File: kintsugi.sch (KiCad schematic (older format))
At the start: 147 parts

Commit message: Footprints added
First revision of the schematic finished and footprints added.
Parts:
- removed D? (x9): D_Small, symbol Device:D_Small
- removed MX? (x10): MX-NoLED, symbol MX_Alps_Hybrid:MX-NoLED
- added C1, C10, C11, C12, C13, C14, C15, C16, C2, C3, C4, C5, C6, C7, C8, C9: 100n, Capacitor_SMD:C_0805_2012Metric_Pad1.18x1.45mm_HandSolder, symbol Device:C_Small
- added D54: D_Small, Diode_THT:D_DO-35_SOD27_P7.62mm_Horizontal, symbol Device:D_Small
- added D66, D67, D68, D69, D70, D71, D72, D73, D74, D75, D76, D77, D78, D79, D80, D81: WS2812B, LED_SMD:LED_WS2812B_PLCC4_5.0x5.0mm_P3.2mm, symbol LED:WS2812B
- added J1: Conn_01x04, Connector_PinHeader_2.54mm:PinHeader_1x04_P2.54mm_Vertical, symbol Connector_Generic:Conn_01x04
- added MX53: MX-NoLED, MX_Only:MXOnly-1.75U-Hotswap, symbol MX_Alps_Hybrid:MX-NoLED
- added SW1: Rotary_Encoder_Switch, Rotary_Encoder:RotaryEncoder_Alps_EC11E-Switch_Vertical_H20mm, symbol Device:Rotary_Encoder_Switch
- D1, D10, D11, D12, D13, D14, D15, D16, D17, D18, D19, D2, D20, D21, D22, D23, D24, D25, D26, D27, D28, D29, D3, D30, D31, D32, D33, D34, D35, D36, D37, D38, D39, D4, D40, D41, D42, D43, D44, D45, D46, D47, D48, D49, D5, D50, D51, D52, D53, D55, D56, D57, D58, D59, D6, D60, D61, D62, D63, D64, D65, D7, D8, D9: renamed from D?; footprint (none) -> Diode_THT:D_DO-35_SOD27_P7.62mm_Horizontal
- MX1, MX10, MX11, MX12, MX13, MX16, MX17, MX18, MX19, MX2, MX20, MX21, MX22, MX23, MX24, MX25, MX26, MX27, MX3, MX30, MX31, MX32, MX33, MX34, MX35, MX36, MX37, MX38, MX39, MX4, MX40, MX43, MX44, MX45, MX46, MX47, MX48, MX49, MX5, MX50, MX51, MX52, MX54, MX55, MX6, MX62, MX63, MX64, MX7, MX8, MX9: renamed from MX?; footprint (none) -> MX_Only:MXOnly-1U-Hotswap
- MX14: renamed from MX?; footprint (none) -> MX_Only:MXOnly-2U-Hotswap
- MX15, MX28: renamed from MX?; footprint (none) -> MX_Only:MXOnly-1.5U-Hotswap
- MX29: renamed from MX?; footprint (none) -> MX_Only:MXOnly-1.75U-Hotswap
- MX41, MX42: renamed from MX?; footprint (none) -> MX_Only:MXOnly-2.25U-Hotswap
- MX56, MX57, MX58, MX60, MX61: renamed from MX?; footprint (none) -> MX_Only:MXOnly-1.25U-Hotswap
- MX59: renamed from MX?; footprint (none) -> MX_Only:MXOnly-6.25U-Hotswap-ReversedStabilizers
- U1: renamed from U?; footprint (none) -> Keebio-Parts:Elite-C
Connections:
- net COL11: now also MX53.1 (COL)
- net COL14: now also SW1.S2
- net ROW0: no longer D42.1 (K)
- net ROW2: now also D42.1 (K)
- net ROW3: now also D54.1 (K)
- net ENCB: now reaches U1.19 (A2/PF5)
- net ENCB: now also SW1.B
- net ENCA: now reaches U1.20 (A3/PF4)
- net ENCA: now also SW1.A
- net VCC: now reaches U1.21 (VCC)
- net VCC: now also C1.2, C10.2, C11.2, C12.2, C13.2, C14.2, C15.2, C16.2, C2.2, C3.2, C4.2, C5.2, C6.2, C7.2, C8.2, C9.2, D66.1 (VDD), D67.1 (VDD), D68.1 (VDD), D69.1 (VDD), D70.1 (VDD), D71.1 (VDD), D72.1 (VDD), D73.1 (VDD), D74.1 (VDD), D75.1 (VDD), D76.1 (VDD), D77.1 (VDD), D78.1 (VDD), D79.1 (VDD), D80.1 (VDD), D81.1 (VDD), J1.3 (Pin_3)
- net GND: now reaches U1.23 (GND)
- net GND: now also U1.3 (GND), U1.4 (GND), C1.1, C10.1, C11.1, C12.1, C13.1, C14.1, C15.1, C16.1, C2.1, C3.1, C4.1, C5.1, C6.1, C7.1, C8.1, C9.1, D66.3 (VSS), D67.3 (VSS), D68.3 (VSS), D69.3 (VSS), D70.3 (VSS), D71.3 (VSS), D72.3 (VSS), D73.3 (VSS), D74.3 (VSS), D75.3 (VSS), D76.3 (VSS), D77.3 (VSS), D78.3 (VSS), D79.3 (VSS), D80.3 (VSS), D81.3 (VSS), J1.4 (Pin_4), SW1.C
- net ULED: now reaches U1.24 (B0)
- net ULED: now also D66.4 (DIN)
- net SDA: now reaches U1.5 (2/PD1)
- net SDA: now also J1.1 (Pin_1)
- net SCL: now reaches U1.6 (3/PD0)
- net SCL: now also J1.2 (Pin_2)
- net RE: now reaches D42.2 (A)
- net RE: now also SW1.S1
- new net: D66.2 (DOUT), D67.4 (DIN)
- new net: D67.2 (DOUT), D68.4 (DIN)
- new net: D68.2 (DOUT), D69.4 (DIN)
- new net: D69.2 (DOUT), D70.4 (DIN)
- new net: D70.2 (DOUT), D71.4 (DIN)
- new net: D71.2 (DOUT), D72.4 (DIN)
- new net: D72.2 (DOUT), D73.4 (DIN)
- new net: D73.2 (DOUT), D74.4 (DIN)
- new net: D74.2 (DOUT), D75.4 (DIN)
- new net: D75.2 (DOUT), D76.4 (DIN)
- new net: D76.2 (DOUT), D77.4 (DIN)
- new net: D77.2 (DOUT), D78.4 (DIN)
- new net: D78.2 (DOUT), D79.4 (DIN)
- new net: D79.2 (DOUT), D80.4 (DIN)
- new net: D80.2 (DOUT), D81.4 (DIN)
- new net: D54.2 (A), MX53.2 (ROW)
- no-connect marks 0 -> 1
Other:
- note added: "Encoder"
- note added: "Matrix"
- note added: "OLED"
- note added: "Underglow"
- moved on the sheet: D1, D10, D11, D12, D13, D14, D15, D16, D17, D18, D19, D2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

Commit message: Routing started
Began routing rows and columns
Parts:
- D1, D10, D11, D12, D13, D14, D15, D16, D17, D18, D19, D2, D20, D21, D22, D23, D24, D25, D26, D27, D28, D29, D3, D30, D31, D32, D33, D34, D35, D36, D37, D38, D39, D4, D40, D41, D42, D43, D44, D45, D46, D47, D48, D49, D5, D50, D51, D52, D53, D54, D55, D56, D57, D58, D59, D6, D60, D61, D62, D63, D64, D65, D7, D8, D9: footprint Diode_THT:D_DO-35_SOD27_P7.62mm_Horizontal -> Keebio-Parts:Diode-dual-onesided

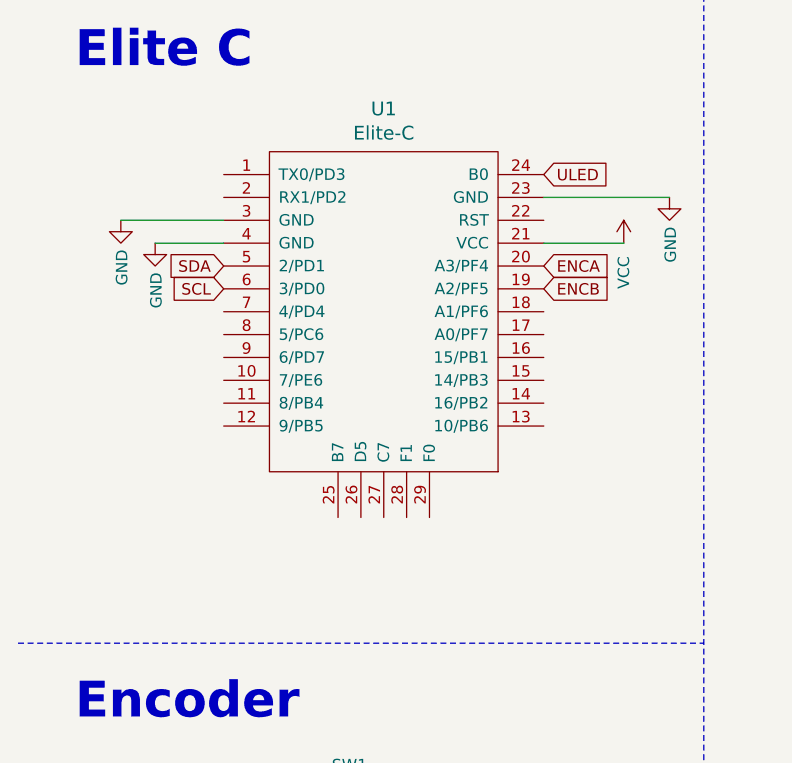
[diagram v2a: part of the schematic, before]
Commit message: Columns and rows connected
Switches connected to their respective row and column
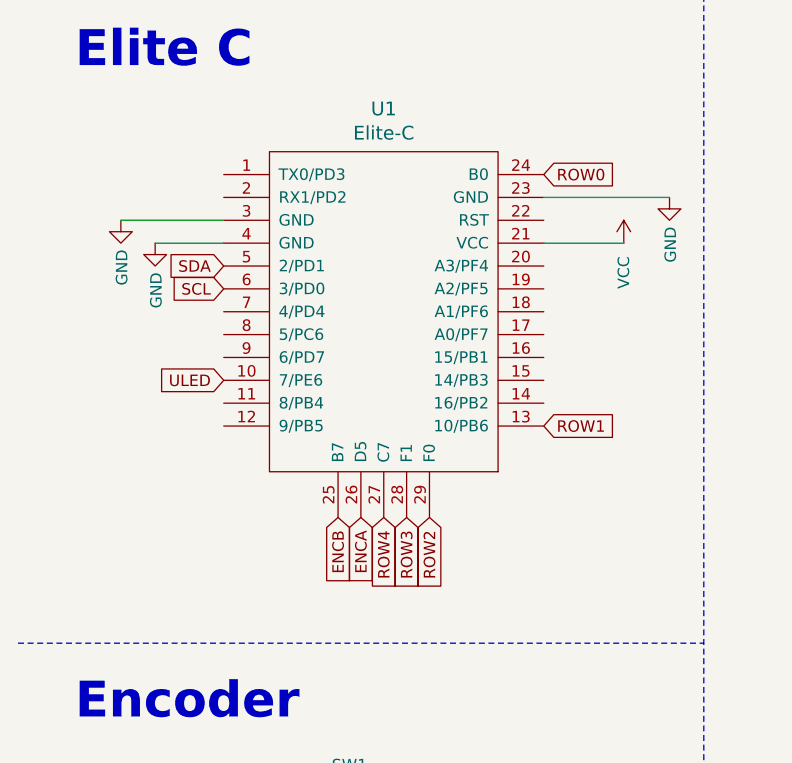
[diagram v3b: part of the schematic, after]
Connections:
- net ENCA: now also U1.26 (D5); no longer U1.20 (A3/PF4)
- net ENCB: now also U1.25 (B7); no longer U1.19 (A2/PF5)
- net ROW0: now also U1.24 (B0)
- net ROW1: now also U1.13 (10/PB6)
- net ROW2: now also U1.29 (F0)
- net ROW3: now also U1.28 (F1)
- net ROW4: now also U1.27 (C7)
- net ULED: now also U1.10 (7/PE6); no longer U1.24 (B0)
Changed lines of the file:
@@
 	1    0    0    -1
 $EndComp
-Text GLabel 2800 1450 2    50   Input ~ 0
+Text GLabel 1400 2350 0    50   Input ~ 0
 ULED
 Text Notes 4200 6700 0    157  ~ 31
@@
 Wire Wire Line
 	11950 8600 12100 8600
-Text GLabel 2800 1950 2    50   Input ~ 0
+Text GLabel 1900 2950 3    50   Input ~ 0
 ENCB
-Text GLabel 2800 1850 2    50   Input ~ 0
+Text GLabel 2000 2950 3    50   Input ~ 0
 ENCA
 $Comp
@@
 RE
 Connection ~ 12850 3950
+Text GLabel 2800 1450 2    50   Input ~ 0
+ROW0
+Text GLabel 2800 2550 2    50   Input ~ 0
+ROW1
+Text GLabel 2300 2950 3    50   Input ~ 0
+ROW2
+Text GLabel 2200 2950 3    50   Input ~ 0
+ROW3
+Text GLabel 2100 2950 3    50   Input ~ 0
+ROW4
 $EndSCHEMATC

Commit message: Routed rows and first three columns
Began routing the new pcb.
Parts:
- removed D10, D24: D_Small, Keebio-Parts:Diode-dual-onesided, symbol Device:D_Small
- removed MX10, MX24: MX-NoLED, MX_Only:MXOnly-1U-Hotswap, symbol MX_Alps_Hybrid:MX-NoLED
- added D13, D27: D_Small, Keebio-Parts:Diode-dual-onesided, symbol Device:D_Small
- added MX13, MX27: MX-NoLED, MX_Only:MXOnly-1U-Hotswap, symbol MX_Alps_Hybrid:MX-NoLED
- renumbered D11 to D10, D12 to D11, D13 to D12, D25 to D24, D26 to D25, D27 to D26, MX11 to MX10, MX12 to MX11, MX13 to MX12, MX25 to MX24, MX26 to MX25, MX27 to MX26
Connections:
- net COL12 is gone; now on net COL4: MX12.1 (COL), MX26.1 (COL), MX62.1 (COL)
- net COL14 is gone; now on net COL6: MX55.1 (COL), MX64.1 (COL), SW1.S2
- net COL7 is gone; now on net COL0: MX22.1 (COL), MX36.1 (COL), MX49.1 (COL), MX8.1 (COL)
- net COL8 is gone; now on net COL1: MX23.1 (COL), MX37.1 (COL), MX50.1 (COL), MX9.1 (COL)
- net COL9 is gone; now on net COL2: MX38.1 (COL), MX51.1 (COL)
- net COL2: now also MX10.1 (COL), MX24.1 (COL), MX60.1 (COL)
- net COL3: now also MX11.1 (COL), MX25.1 (COL), MX39.1 (COL), MX52.1 (COL), MX61.1 (COL)
- net COL4: now also MX40.1 (COL), MX53.1 (COL)
- net COL5: now also MX41.1 (COL), MX54.1 (COL), MX63.1 (COL), MX13.1 (COL), MX27.1 (COL)
- net COL6: now also MX14.1 (COL), MX28.1 (COL)
- net ROW0: no longer D10.1 (K), D11.1 (K), D12.1 (K), D14.1 (K), D8.1 (K), D9.1 (K)
- net ROW1: no longer D22.1 (K), D23.1 (K), D24.1 (K), D25.1 (K), D26.1 (K), D28.1 (K)
- net ROW2: no longer D36.1 (K), D37.1 (K), D38.1 (K), D39.1 (K), D40.1 (K), D41.1 (K), D42.1 (K)
- net ROW3: no longer D50.1 (K), D51.1 (K), D52.1 (K), D53.1 (K), D54.1 (K), D55.1 (K), D56.1 (K)
- net ROW4: no longer D61.1 (K), D62.1 (K), D63.1 (K), D64.1 (K), D65.1 (K)
- removed net COL10: MX10.1 (COL), MX24.1 (COL), MX39.1 (COL), MX52.1 (COL), MX60.1 (COL)
- removed net COL11: MX11.1 (COL), MX25.1 (COL), MX40.1 (COL), MX53.1 (COL), MX61.1 (COL)
- removed net COL13: MX14.1 (COL), MX28.1 (COL), MX41.1 (COL), MX54.1 (COL), MX63.1 (COL)
- new net: D13.2 (A), MX13.2 (ROW)
- new net: D27.2 (A), MX27.2 (ROW)
- new net ROW5: D10.1 (K), D11.1 (K), D12.1 (K), D13.1 (K), D14.1 (K), D8.1 (K), D9.1 (K)
- new net ROW6: D22.1 (K), D23.1 (K), D24.1 (K), D25.1 (K), D26.1 (K), D27.1 (K), D28.1 (K)
- new net ROW7: D36.1 (K), D37.1 (K), D38.1 (K), D39.1 (K), D40.1 (K), D41.1 (K), D42.1 (K)
- new net ROW8: D50.1 (K), D51.1 (K), D52.1 (K), D53.1 (K), D54.1 (K), D55.1 (K), D56.1 (K)
- new net ROW9: D61.1 (K), D62.1 (K), D63.1 (K), D64.1 (K), D65.1 (K)
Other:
- moved on the sheet: C1, C10, C11, C12, C13, C14, C15, C16, C2, C3, C4, C5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

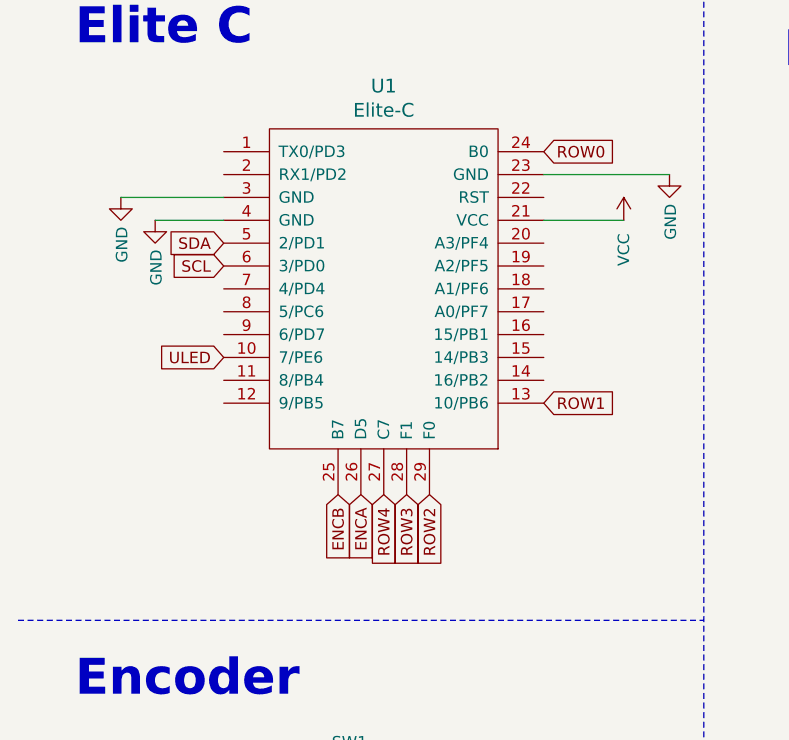
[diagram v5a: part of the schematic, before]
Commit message: Routed first 5 rows
Finished routing leds and first 5 rows
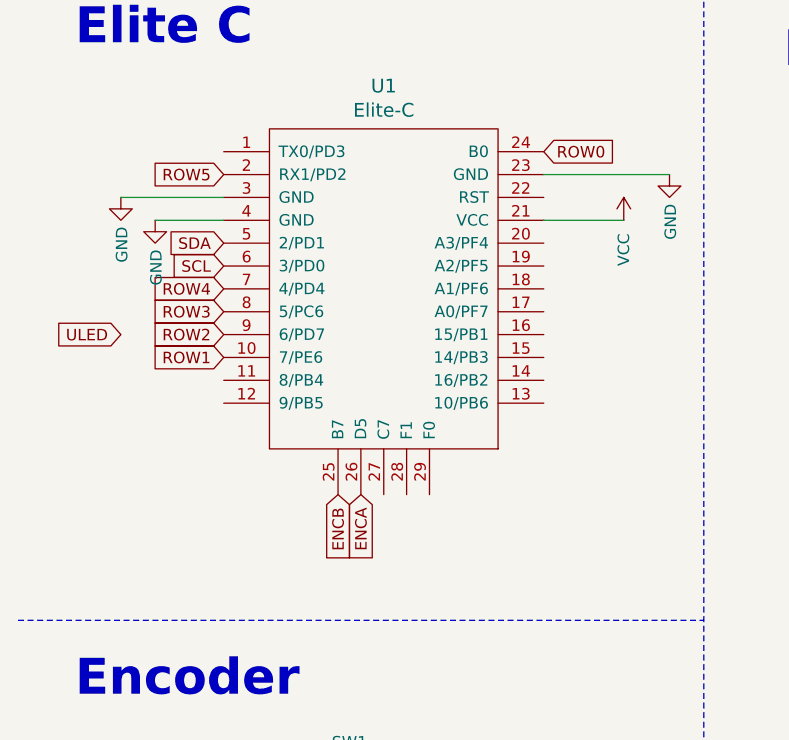
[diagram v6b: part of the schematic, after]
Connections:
- net ROW1: now also U1.10 (7/PE6); no longer U1.13 (10/PB6)
- net ROW2: now also U1.9 (6/PD7); no longer U1.29 (F0)
- net ROW3: now also U1.8 (5/PC6); no longer U1.28 (F1)
- net ROW4: now also U1.7 (4/PD4); no longer U1.27 (C7)
- net ROW5: now also U1.2 (RX1/PD2)
- net ULED: no longer U1.10 (7/PE6)
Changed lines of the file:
@@
 Text GLabel 1400 1950 0    50   Input ~ 0
 SCL
-Text GLabel 1400 2350 0    50   Input ~ 0
+Text GLabel 950  2250 0    50   Input ~ 0
 ULED
 $Bitmap
@@
 Text GLabel 2800 1450 2    50   Input ~ 0
 ROW0
-Text GLabel 2800 2550 2    50   Input ~ 0
-ROW1
-Text GLabel 2100 2950 3    50   Input ~ 0
+Text GLabel 1400 2050 0    50   Input ~ 0
 ROW4
-Text GLabel 2200 2950 3    50   Input ~ 0
-ROW3
-Text GLabel 2300 2950 3    50   Input ~ 0
-ROW2
 Text GLabel 2000 2950 3    50   Input ~ 0
 ENCA
 Text GLabel 1900 2950 3    50   Input ~ 0
 ENCB
+Text GLabel 1400 1550 0    50   Input ~ 0
+ROW5
+Text GLabel 1400 2350 0    50   Input ~ 0
+ROW1
+Text GLabel 1400 2150 0    50   Input ~ 0
+ROW3
+Text GLabel 1400 2250 0    50   Input ~ 0
+ROW2
 $EndSCHEMATC

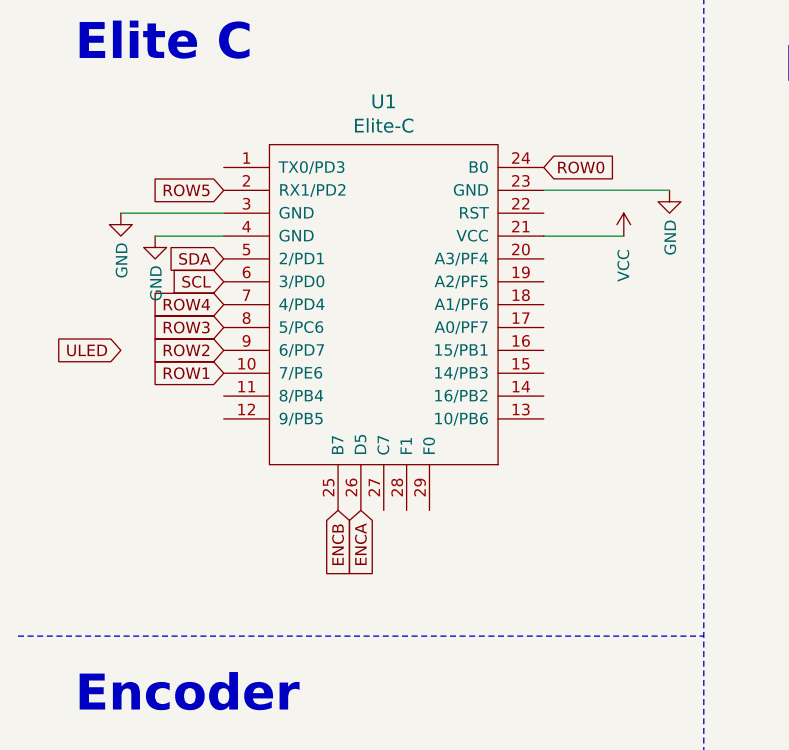
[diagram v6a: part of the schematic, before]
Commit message: Finished routing and gnd fill
First revision completed, waiting for review
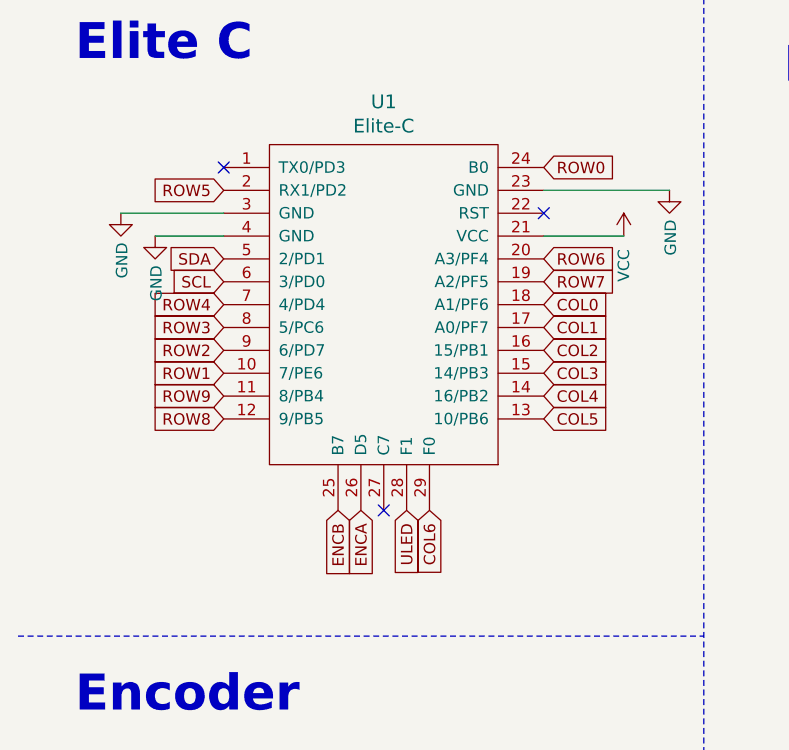
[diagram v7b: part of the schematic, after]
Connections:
- net COL0: now also U1.18 (A1/PF6)
- net COL1: now also U1.17 (A0/PF7)
- net COL2: now also U1.16 (15/PB1)
- net COL3: now also U1.15 (14/PB3)
- net COL4: now also U1.14 (16/PB2)
- net COL5: now also U1.13 (10/PB6)
- net COL6: now also U1.29 (F0)
- net ROW6: now also U1.20 (A3/PF4)
- net ROW7: now also U1.19 (A2/PF5)
- net ROW8: now also U1.12 (9/PB5)
- net ROW9: now also U1.11 (8/PB4)
- net ULED: now also U1.28 (F1)
- no-connect marks 1 -> 4
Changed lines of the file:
@@
 Text GLabel 1400 1950 0    50   Input ~ 0
 SCL
-Text GLabel 950  2250 0    50   Input ~ 0
+Text GLabel 2200 2950 3    50   Input ~ 0
 ULED
 $Bitmap
@@
 $EndBitmap
 $Comp
-L keebio:Elite-C U1
-U 1 1 612AFD7E
-P 2100 2000
-F 0 "U1" H 2100 2837 60  0000 C CNN
-F 1 "Elite-C" H 2100 2731 60  0000 C CNN
-F 2 "Keebio-Parts:Elite-C" V 3150 -500 60  0001 C CNN
-F 3 "" V 3150 -500 60  0001 C CNN
-	1    2100 2000
-	1    0    0    -1
-$EndComp
-$Comp
 L power:GND #PWR01
 U 1 1 619FD96C
@@
 Text GLabel 1400 2250 0    50   Input ~ 0
 ROW2
+Text GLabel 2800 1850 2    50   Input ~ 0
+ROW6
+Text GLabel 2800 1950 2    50   Input ~ 0
+ROW7
+Text GLabel 1400 2550 0    50   Input ~ 0
+ROW8
+Text GLabel 1400 2450 0    50   Input ~ 0
+ROW9
+Text GLabel 2800 2050 2    50   Input ~ 0
+COL0
+Text GLabel 2800 2150 2    50   Input ~ 0
+COL1
+Text GLabel 2800 2250 2    50   Input ~ 0
+COL2
+Text GLabel 2800 2350 2    50   Input ~ 0
+COL3
+$Comp
+L keebio:Elite-C U1
+U 1 1 612AFD7E
+P 2100 2000
+F 0 "U1" H 2100 2837 60  0000 C CNN
+F 1 "Elite-C" H 2100 2731 60  0000 C CNN
+F 2 "Keebio-Parts:Elite-C" V 3150 -500 60  0001 C CNN
+F 3 "" V 3150 -500 60  0001 C CNN
+	1    2100 2000
+	1    0    0    -1
+$EndComp
+Text GLabel 2800 2450 2    50   Input ~ 0
+COL4
+Text GLabel 2800 2550 2    50   Input ~ 0
+COL5
+Text GLabel 2300 2950 3    50   Input ~ 0
+COL6
+NoConn ~ 1400 1450
+NoConn ~ 2800 1650
+NoConn ~ 2100 2950
 $EndSCHEMATC
